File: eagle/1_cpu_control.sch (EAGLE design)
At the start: 41 parts, among them IC1 74LS08N, IC10 74LS173N, IC11 74LS273N, IC12 74LS74N, IC13 74LS157N, IC14 74LS157N, IC2 74LS163, IC3 74LS163, IC4 74LS00N, IC5 74LS273N, IC6 74LS148N, IC7 74LS148N, IC8 74LS08N, IC9 74S32N

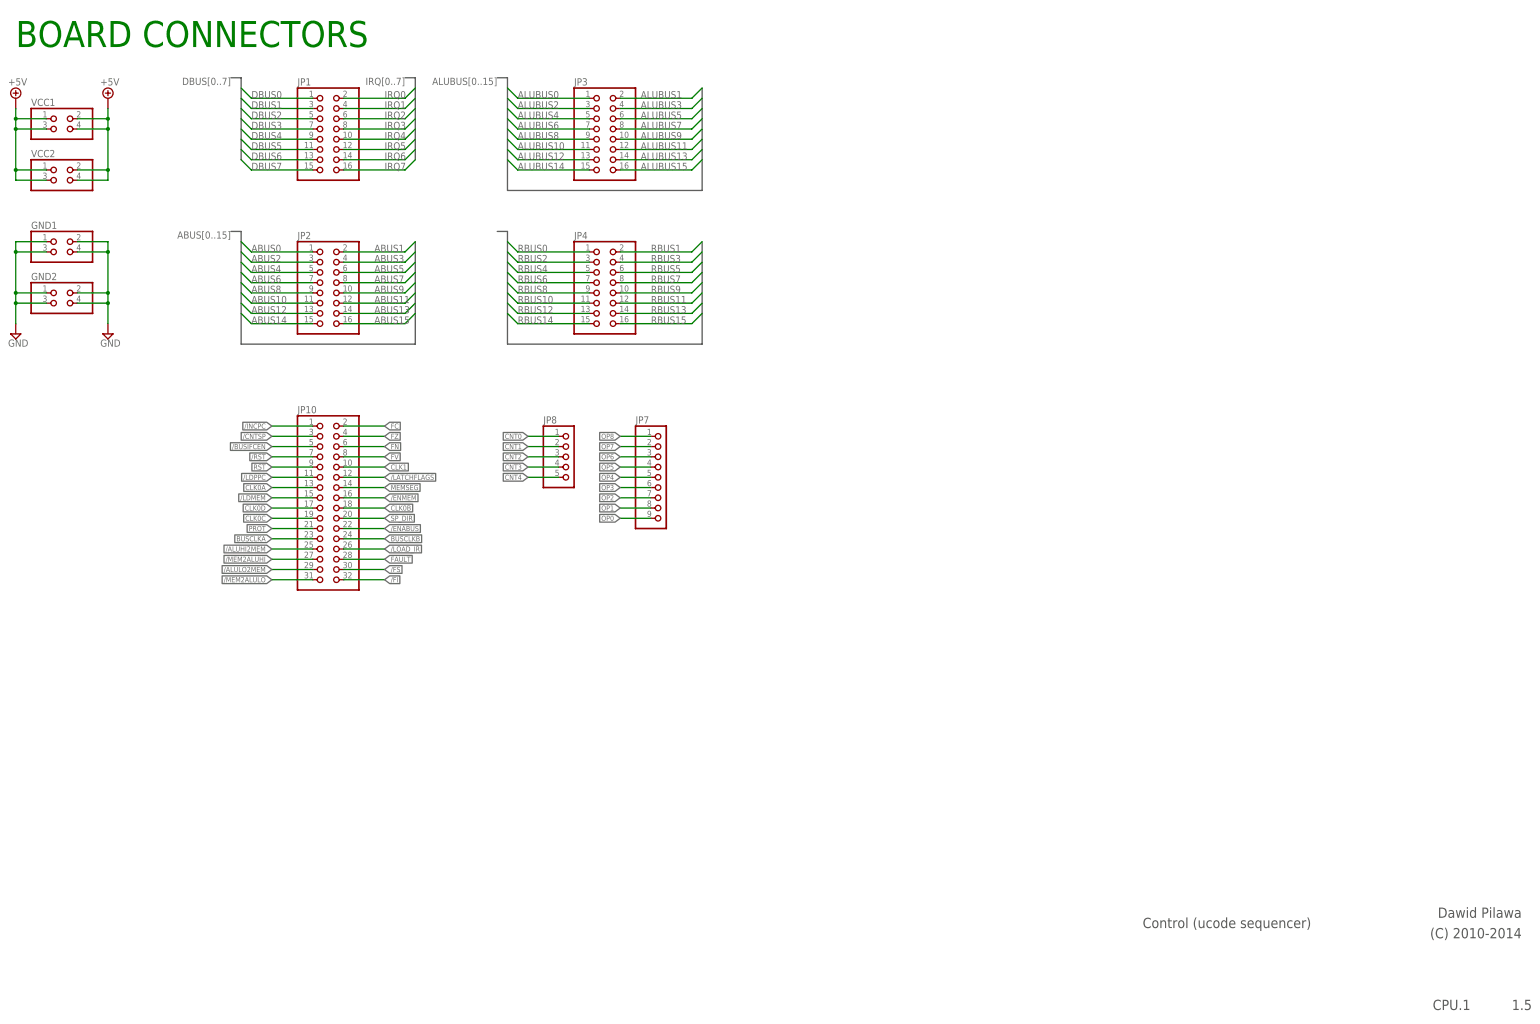
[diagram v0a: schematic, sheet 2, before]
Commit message: All boards prepared for MMU extension
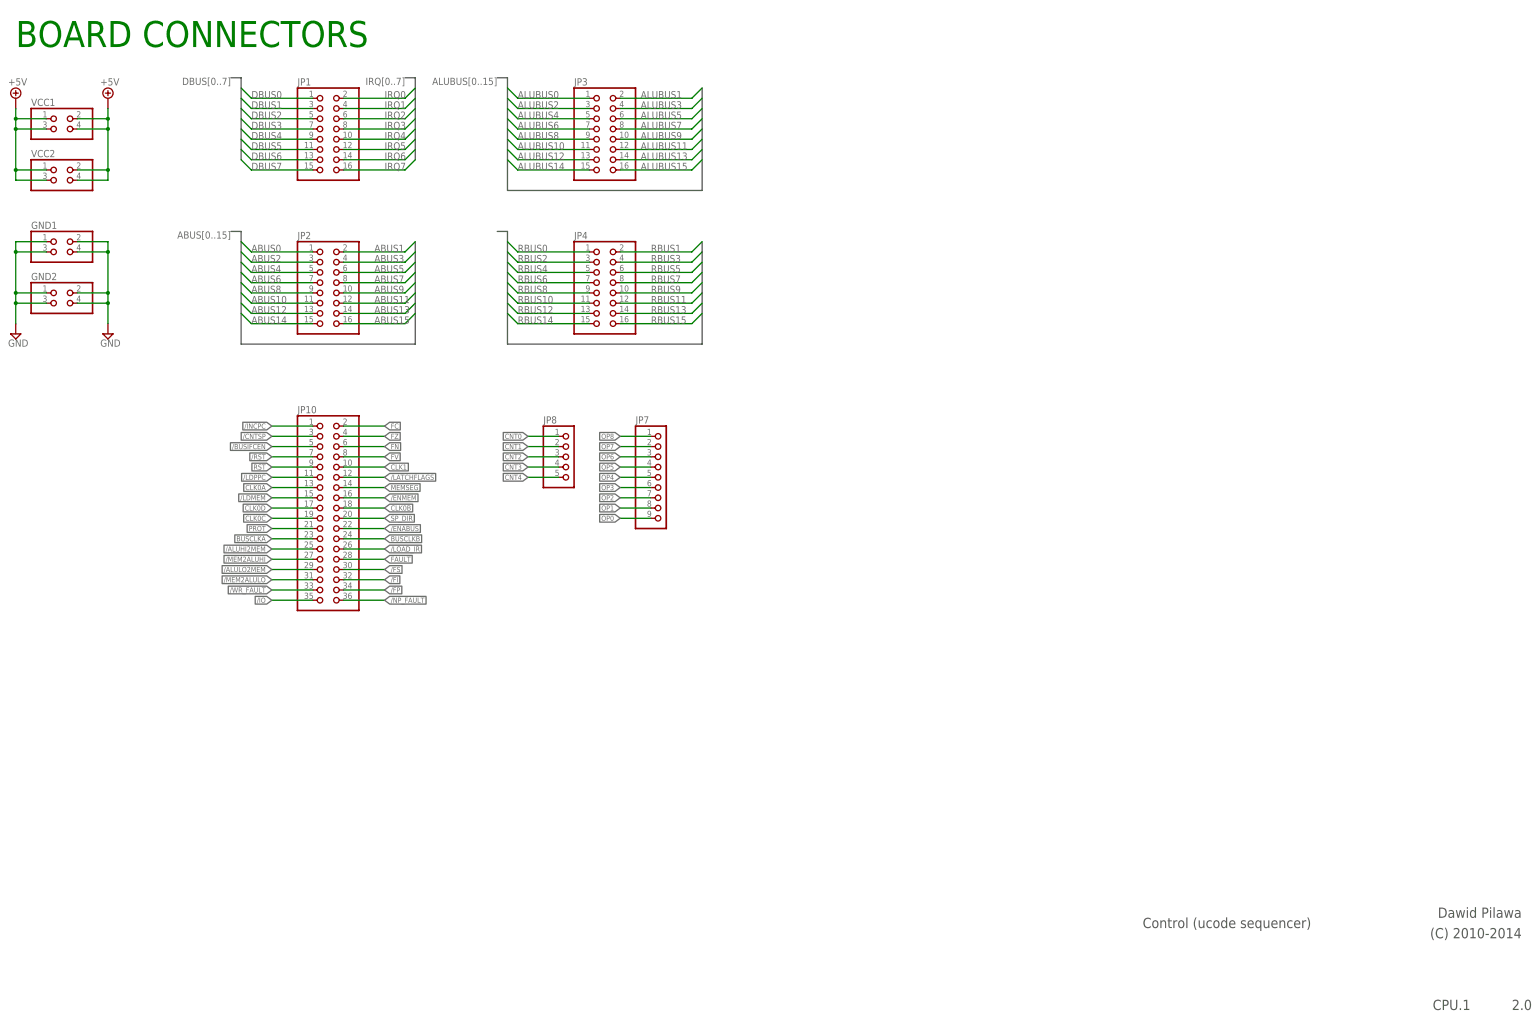
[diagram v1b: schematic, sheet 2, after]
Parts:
- JP10: device pinhead:PINHD-2X16 -> pinhead:PINHD-2X18
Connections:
- new net /FP: JP10.34
- new net /IO: JP10.35
- new net /NP_FAULT: IC7A.6, JP10.36
- new net /WR_FAULT: IC7A.5, JP10.33
- net +5V: no longer IC7A.5, IC7A.6
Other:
- note added: "2.0"
- note removed: "1.5"
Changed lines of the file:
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@@
 <part name="JP3" library="pinhead" deviceset="PINHD-2X8" device=""/>
 <part name="JP4" library="pinhead" deviceset="PINHD-2X8" device=""/>
-<part name="JP10" library="pinhead" deviceset="PINHD-2X16" device=""/>
+<part name="JP10" library="pinhead" deviceset="PINHD-2X18" device=""/>
 <part name="JP8" library="pinhead" deviceset="PINHD-1X5" device=""/>
 <part name="JP7" library="pinhead" deviceset="PINHD-1X9" device=""/>
@@
 <plain>
 <text x="289.56" y="27.94" size="2.54" layer="97" font="vector">Control (ucode sequencer)</text>
-<text x="386.08" y="10.16" size="2.54" layer="97" font="vector" rot="R180">1.5</text>
+<text x="386.08" y="10.16" size="2.54" layer="97" font="vector" rot="R180">2.0</text>
 <text x="383.54" y="33.02" size="2.54" layer="97" font="vector" rot="R180">Dawid Pilawa</text>
 <text x="383.54" y="27.94" size="2.54" layer="97" font="vector" rot="R180">(C) 2010-2014</text>
@@
 <wire x1="177.8" y1="185.42" x2="177.8" y2="182.88" width="0.1524" layer="91"/>
 <wire x1="180.34" y1="182.88" x2="177.8" y2="182.88" width="0.1524" layer="91"/>
-<wire x1="177.8" y1="182.88" x2="177.8" y2="180.34" width="0.1524" layer="91"/>
-<wire x1="180.34" y1="180.34" x2="177.8" y2="180.34" width="0.1524" layer="91"/>
-<wire x1="177.8" y1="180.34" x2="177.8" y2="177.8" width="0.1524" layer="91"/>
-<wire x1="180.34" y1="177.8" x2="177.8" y2="177.8" width="0.1524" layer="91"/>
 <wire x1="177.8" y1="190.5" x2="177.8" y2="193.04" width="0.1524" layer="91"/>
 <junction x="177.8" y="187.96"/>
 <junction x="177.8" y="185.42"/>
-<junction x="177.8" y="182.88"/>
-<junction x="177.8" y="180.34"/>
 <junction x="177.8" y="190.5"/>
 <junction x="177.8" y="193.04"/>
@@
 <pinref part="IC7" gate="A" pin="3"/>
 <pinref part="IC7" gate="A" pin="4"/>
-<pinref part="IC7" gate="A" pin="5"/>
-<pinref part="IC7" gate="A" pin="6"/>
 <pinref part="IC7" gate="A" pin="0"/>
 </segment>
@@
 </segment>
 </net>
+<net name="/NP_FAULT" class="0">
+<segment>
+<pinref part="IC7" gate="A" pin="6"/>
+<wire x1="180.34" y1="177.8" x2="177.8" y2="177.8" width="0.1524" layer="91"/>
+<label x="177.8" y="177.8" size="1.27" layer="95" rot="R180" xref="yes"/>
+</segment>
+</net>
+<net name="/WR_FAULT" class="0">
+<segment>
+<pinref part="IC7" gate="A" pin="5"/>
+<wire x1="180.34" y1="180.34" x2="177.8" y2="180.34" width="0.1524" layer="91"/>
+<label x="177.8" y="180.34" size="1.27" layer="95" rot="R180" xref="yes"/>
+</segment>
+</net>
 </nets>
 </sheet>
@@
 <plain>
 <text x="289.56" y="27.94" size="2.54" layer="97" font="vector">Control (ucode sequencer)</text>
-<text x="386.08" y="10.16" size="2.54" layer="97" font="vector" rot="R180">1.5</text>
+<text x="386.08" y="10.16" size="2.54" layer="97" font="vector" rot="R180">2.0</text>
 <text x="383.54" y="33.02" size="2.54" layer="97" font="vector" rot="R180">Dawid Pilawa</text>
 <text x="383.54" y="27.94" size="2.54" layer="97" font="vector" rot="R180">(C) 2010-2014</text>
@@
 <instance part="JP3" gate="A" x="154.94" y="226.06"/>
 <instance part="JP4" gate="A" x="154.94" y="187.96"/>
-<instance part="JP10" gate="A" x="86.36" y="134.62"/>
+<instance part="JP10" gate="A" x="86.36" y="132.08"/>
 <instance part="JP8" gate="A" x="147.32" y="144.78"/>
 <instance part="JP7" gate="A" x="170.18" y="139.7"/>
@@
 </segment>
 </net>
+<net name="/FP" class="0">
+<segment>
+<pinref part="JP10" gate="A" pin="34"/>
+<wire x1="91.44" y1="111.76" x2="101.6" y2="111.76" width="0.1524" layer="91"/>
+<label x="101.6" y="111.76" size="1.27" layer="95" xref="yes"/>
+</segment>
+</net>
+<net name="/WR_FAULT" class="0">
+<segment>
+<pinref part="JP10" gate="A" pin="33"/>
+<wire x1="83.82" y1="111.76" x2="73.66" y2="111.76" width="0.1524" layer="91"/>
+<label x="73.66" y="111.76" size="1.27" layer="95" rot="R180" xref="yes"/>
+</segment>
+</net>
+<net name="/NP_FAULT" class="0">
+<segment>
+<pinref part="JP10" gate="A" pin="36"/>
+<wire x1="91.44" y1="109.22" x2="101.6" y2="109.22" width="0.1524" layer="91"/>
+<label x="101.6" y="109.22" size="1.27" layer="95" xref="yes"/>
+</segment>
+</net>
+<net name="/IO" class="0">
+<segment>
+<pinref part="JP10" gate="A" pin="35"/>
+<wire x1="83.82" y1="109.22" x2="73.66" y2="109.22" width="0.1524" layer="91"/>
+<label x="73.66" y="109.22" size="1.27" layer="95" rot="R180" xref="yes"/>
+</segment>
+</net>

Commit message: Removal of PPC started
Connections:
- removed net /LDPPC: IC11A.CLK, IC12A.CLK, IC9D.O, JP10.11
- new net N$15: IC1A.O, IC1B.I0
- new net N$17: IC11A.CLK, IC12A.CLK, IC9D.O
- new net N$8: IC2A.CLR, IC3A.CLR
- net +5V: no longer IC1B.I0, IC1B.I1
- net /NEXTOP: now also IC1B.O; no longer IC1A.O, IC2A.CLR, IC3A.CLR
- net N$10: now also IC1B.I1
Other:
- moved on the sheet: IC1A, IC1B, IC4D, IC9D
